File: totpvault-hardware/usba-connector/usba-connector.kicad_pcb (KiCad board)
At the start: 2 copper layers, 17.1 x 37.8 mm, 30 parts, among them J3 Conn_01x06_Socket, U1 ESP32-C3, U2 HT75xx-1-SOT89, U3 CH343P, U4 USBLC6-2SC6, Y1 Crystal_GND24

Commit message: Finalized PCB, added label and fixed solder mask
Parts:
- moved J3 1.10 mm to (99.0, 55.8)
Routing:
- net TXD_uC: track 23.8 -> 24.5 mm
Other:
- board text added: "PassVault v1.0"
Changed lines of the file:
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@@
 	(footprint "Connector_PinHeader_2.54mm:PinHeader_1x06_P2.54mm_Vertical"
 		(layer "F.Cu")
-		(at 98.975 56.85)
+		(at 99 55.75)
 		(descr "Through hole straight pin header, 1x06, 2.54mm pitch, single row")
 		(tags "Through hole pin header THT 1x06 2.54mm single row")
 		(property "Reference" "J3"
-			(at 0 -2.33 0)
+			(at -0.9 -2.25 0)
 			(layer "F.SilkS")
 			(effects
@@
 		(tags "SMD SMT crystal")
 		(property "Reference" "Y1"
-			(at 2.5 -2 0)
+			(at -0.2 2.15 0)
 			(layer "F.SilkS")
 			(effects
@@
 		(at 100.945 51.25 180)
 		(property "Reference" "U3"
-			(at 2.445 -0.25 270)
+			(at 2.445 0.05 90)
 			(layer "F.SilkS")
 			(effects
@@
 		(sheetname "/")
 		(sheetfile "usba-connector.kicad_sch")
+		(solder_mask_margin 0)
 		(attr smd)
 		(fp_line
@@
 			(pinfunction "VIO")
 			(pintype "power_in")
-			(solder_mask_margin 0.07)
+			(solder_mask_margin 0.01)
 			(clearance 0.07)
 		)
@@
 			(pinfunction "GND")
 			(pintype "power_in")
-			(solder_mask_margin 0.07)
+			(solder_mask_margin 0.01)
 			(clearance 0.07)
 		)
@@
 			(pinfunction "VDD5")
 			(pintype "power_in")
-			(solder_mask_margin 0.07)
+			(solder_mask_margin 0.01)
 			(clearance 0.07)
 		)
@@
 			(pinfunction "TXD")
 			(pintype "output")
-			(solder_mask_margin 0.07)
+			(solder_mask_margin 0.01)
 			(clearance 0.07)
 		)
@@
 			(pinfunction "RXD")
 			(pintype "input")
-			(solder_mask_margin 0.07)
+			(solder_mask_margin 0.01)
 			(clearance 0.07)
 		)
@@
 			(pinfunction "V3")
 			(pintype "power_in")
-			(solder_mask_margin 0.07)
+			(solder_mask_margin 0.01)
 			(clearance 0.07)
 		)
@@
 			(pinfunction "UD+")
 			(pintype "bidirectional")
-			(solder_mask_margin 0.07)
+			(solder_mask_margin 0.01)
 			(clearance 0.07)
 		)
@@
 			(pinfunction "UD-")
 			(pintype "bidirectional")
-			(solder_mask_margin 0.07)
+			(solder_mask_margin 0.01)
 			(clearance 0.07)
 		)
@@
 			(pinfunction "VBUS")
 			(pintype "input")
-			(solder_mask_margin 0.07)
+			(solder_mask_margin 0.01)
 			(clearance 0.07)
 		)
@@
 			(pinfunction "~{ACT}")
 			(pintype "output+no_connect")
-			(solder_mask_margin 0.07)
+			(solder_mask_margin 0.01)
 			(clearance 0.07)
 		)
@@
 			(pinfunction "DCD")
 			(pintype "input+no_connect")
-			(solder_mask_margin 0.07)
+			(solder_mask_margin 0.01)
 			(clearance 0.07)
 		)
@@
 			(pinfunction "DTR")
 			(pintype "output+no_connect")
-			(solder_mask_margin 0.07)
+			(solder_mask_margin 0.01)
 			(clearance 0.07)
 		)
@@
 			(pinfunction "RTS")
 			(pintype "output+no_connect")
-			(solder_mask_margin 0.07)
+			(solder_mask_margin 0.01)
 			(clearance 0.07)
 		)
@@
 			(pinfunction "DSR")
 			(pintype "input+no_connect")
-			(solder_mask_margin 0.07)
+			(solder_mask_margin 0.01)
 			(clearance 0.07)
 		)
@@
 			(pinfunction "CTS")
 			(pintype "input+no_connect")
-			(solder_mask_margin 0.07)
+			(solder_mask_margin 0.01)
 			(clearance 0.07)
 		)
@@
 			(pinfunction "RI")
 			(pintype "input+no_connect")
-			(solder_mask_margin 0.07)
+			(solder_mask_margin 0.01)
 			(clearance 0.07)
 		)
@@
 			(pinfunction "GND__1")
 			(pintype "power_in")
-			(solder_mask_margin 0.07)
+			(solder_mask_margin 0)
 			(clearance 0.07)
 		)
@@
 		(tags "LED")
 		(property "Reference" "D1"
-			(at 1.975 0 90)
+			(at -0.3 1.275 90)
 			(layer "F.SilkS")
 			(effects
@@
 		(layer "Edge.Cuts")
 	)
+	(gr_text "PassVault v1.0"
+		(at 101.3 71 0)
+		(layer "F.SilkS")
+		(effects
+			(font
+				(size 0.8 0.8)
+				(thickness 0.16)
+				(bold yes)
+			)
+			(justify left bottom)
+		)
+	)
 	(segment
 		(start 103.205 48.125)
@@
 	)
 	(segment
+		(start 104.758944 54.65)
+		(end 105.616972 53.791972)
+		(width 0.5)
+		(layer "F.Cu")
+		(net 6)
+	)
+	(segment
 		(start 107.545 55.875)
 		(end 107.545 53.685)
@@
 	)
 	(segment
-		(start 108.25 51.375)
-		(end 109.575 52.7)
+		(start 102.375 54.65)
+		(end 104.758944 54.65)
 		(width 0.5)
 		(layer "F.Cu")
@@
 	)
 	(segment
-		(start 98.975 59.39)
-		(end 101.1 57.265)
+		(start 108.25 51.375)
+		(end 109.575 52.7)
 		(width 0.5)
 		(layer "F.Cu")
@@
 	)
 	(segment
-		(start 101.1 57.265)
-		(end 101.1 55.925)
-		(width 0.5)
+		(start 104.345 52.52)
+		(end 105.616972 53.791972)
+		(width 0.2)
 		(layer "F.Cu")
 		(net 6)
 	)
 	(segment
-		(start 104.345 52.52)
-		(end 105.616972 53.791972)
-		(width 0.2)
+		(start 101.1 57.265)
+		(end 100.025 57.265)
+		(width 0.5)
 		(layer "F.Cu")
 		(net 6)
@@
 	)
 	(segment
-		(start 104.758944 54.65)
-		(end 105.616972 53.791972)
+		(start 100.025 57.265)
+		(end 99 58.29)
 		(width 0.5)
 		(layer "F.Cu")
@@
 	)
 	(segment
+		(start 101.1 57.265)
+		(end 101.1 55.925)
+		(width 0.5)
+		(layer "F.Cu")
+		(net 6)
+	)
+	(segment
 		(start 112.525 68.8375)
 		(end 111.1625 68.8375)
@@
 	)
 	(segment
-		(start 102.375 54.65)
-		(end 104.758944 54.65)
+		(start 101.535 57.7)
+		(end 101.1 57.265)
+		(width 0.2)
+		(layer "F.Cu")
+		(net 6)
+	)
+	(segment
+		(start 101.1 55.925)
+		(end 102.375 54.65)
 		(width 0.5)
 		(layer "F.Cu")
@@
 	)
 	(segment
-		(start 101.535 57.7)
-		(end 101.1 57.265)
-		(width 0.2)
-		(layer "F.Cu")
-		(net 6)
-	)
-	(segment
 		(start 108.5 61)
 		(end 110.67 61)
@@
 	)
 	(segment
-		(start 101.1 55.925)
-		(end 102.375 54.65)
-		(width 0.5)
-		(layer "F.Cu")
-		(net 6)
-	)
-	(segment
 		(start 108.25 45.525)
 		(end 108.25 51.375)
@@
 	)
 	(segment
-		(start 99.225 69.8)
-		(end 98.975 69.55)
+		(start 100.35 69.8)
+		(end 99 68.45)
 		(width 0.2)
 		(layer "B.Cu")
@@
 	(segment
 		(start 111.15 69.8)
-		(end 99.225 69.8)
+		(end 100.35 69.8)
 		(width 0.2)
 		(layer "B.Cu")
@@
 	)
 	(segment
+		(start 99.827179 64.197179)
+		(end 99 63.37)
+		(width 0.2)
+		(layer "F.Cu")
+		(net 10)
+	)
+	(segment
 		(start 103.6 49.125)
 		(end 102.375 49.125)
@@
 	)
 	(segment
-		(start 102.659764 64.25)
-		(end 99.195 64.25)
+		(start 102.712585 64.197179)
+		(end 99.827179 64.197179)
 		(width 0.2)
 		(layer "F.Cu")
@@
 	)
 	(segment
-		(start 99.195 64.25)
-		(end 98.975 64.47)
-		(width 0.2)
-		(layer "F.Cu")
-		(net 10)
-	)
-	(segment
 		(start 105.7135 62.8786)
 		(end 105.7135 62.874)
@@
 	)
 	(segment
-		(start 101.75 56.65)
-		(end 101.75 64.235)
+		(start 101.75 64.25)
+		(end 101.75 56.65)
 		(width 0.2)
 		(layer "B.Cu")
@@
 	)
 	(segment
-		(start 102.4 56)
-		(end 101.75 56.65)
+		(start 99 65.91)
+		(end 100.09 65.91)
 		(width 0.2)
 		(layer "B.Cu")
@@
 	(segment
 		(start 103.275 56)
-		(end 102.4 56)
+		(end 103.55 55.725)
+		(width 0.2)
+		(layer "B.Cu")
+		(net 11)
+	)
+	(segment
+		(start 100.09 65.91)
+		(end 101.75 64.25)
 		(width 0.2)
 		(layer "B.Cu")
@@
 	)
 	(segment
-		(start 101.75 64.235)
-		(end 98.975 67.01)
+		(start 101.75 56.65)
+		(end 102.4 56)
 		(width 0.2)
 		(layer "B.Cu")
@@
 	)
 	(segment
-		(start 103.55 55.725)
+		(start 102.4 56)
 		(end 103.275 56)
 		(width 0.2)
@@
 	)
 	(segment
-		(start 105.3125 62.7125)
-		(end 105.3125 62.1875)
+		(start 103.5 63.45)
+		(end 101.05 63.45)
 		(width 0.2)
 		(layer "F.Cu")
@@
 	)
 	(segment
-		(start 100.495 63.45)
-		(end 98.975 61.93)
+		(start 105.3125 62.7125)
+		(end 105.3125 62.1875)
 		(width 0.2)
 		(layer "F.Cu")
@@
 	)
 	(segment
+		(start 99 61.4)
+		(end 99 60.83)
+		(width 0.2)
+		(layer "F.Cu")
+		(net 43)
+	)
+	(segment
 		(start 103.5 63.45)
 		(end 104.575 63.45)
@@
 	)
 	(segment
-		(start 103.5 63.45)
-		(end 100.495 63.45)
+		(start 101.05 63.45)
+		(end 99 61.4)
 		(width 0.2)
 		(layer "F.Cu")

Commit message: PCB Order
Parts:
- removed R2: 499, Resistor_SMD:R_0402_1005Metric
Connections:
- J3 pad 3: TXD_uC -> TXD
- U1 pad 27: TXD_uC -> TXD
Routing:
- net TXD: track 1.59 -> 26.2 mm, vias 0 -> 2
- net TXD_uC: track 24.5 -> 0.00 mm, vias 2 -> 0
- net VBUS: track 55.1 -> 56.0 mm

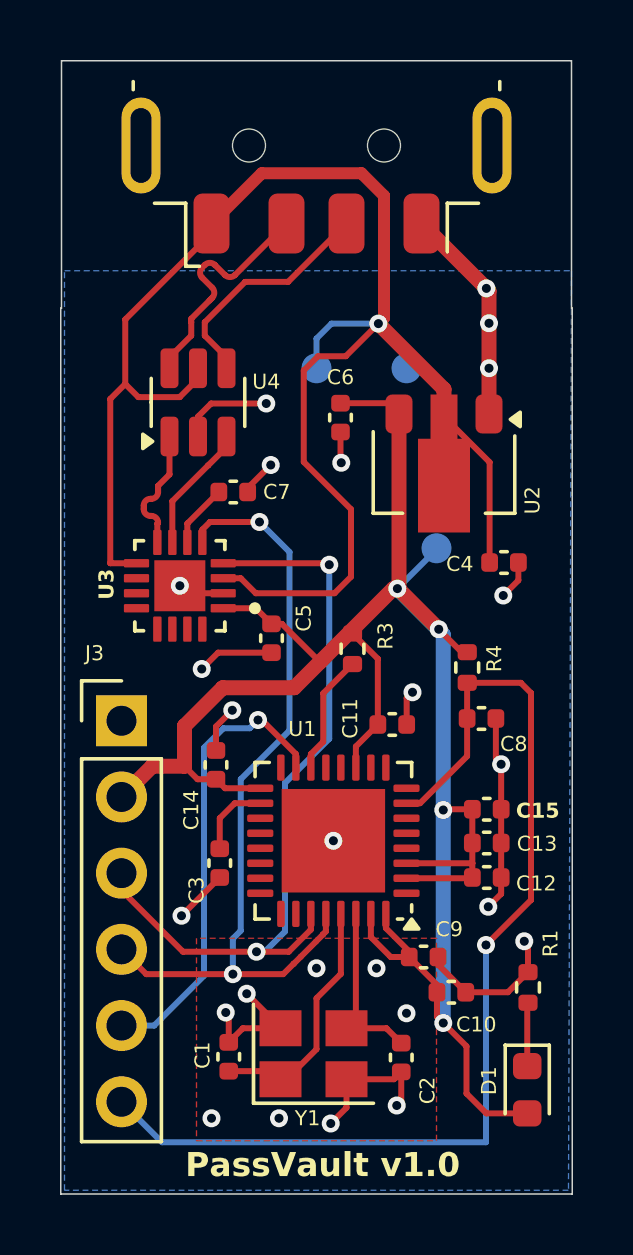
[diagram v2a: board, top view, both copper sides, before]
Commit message: Finalized new board design with JLCPCB basic parts, code cleanup
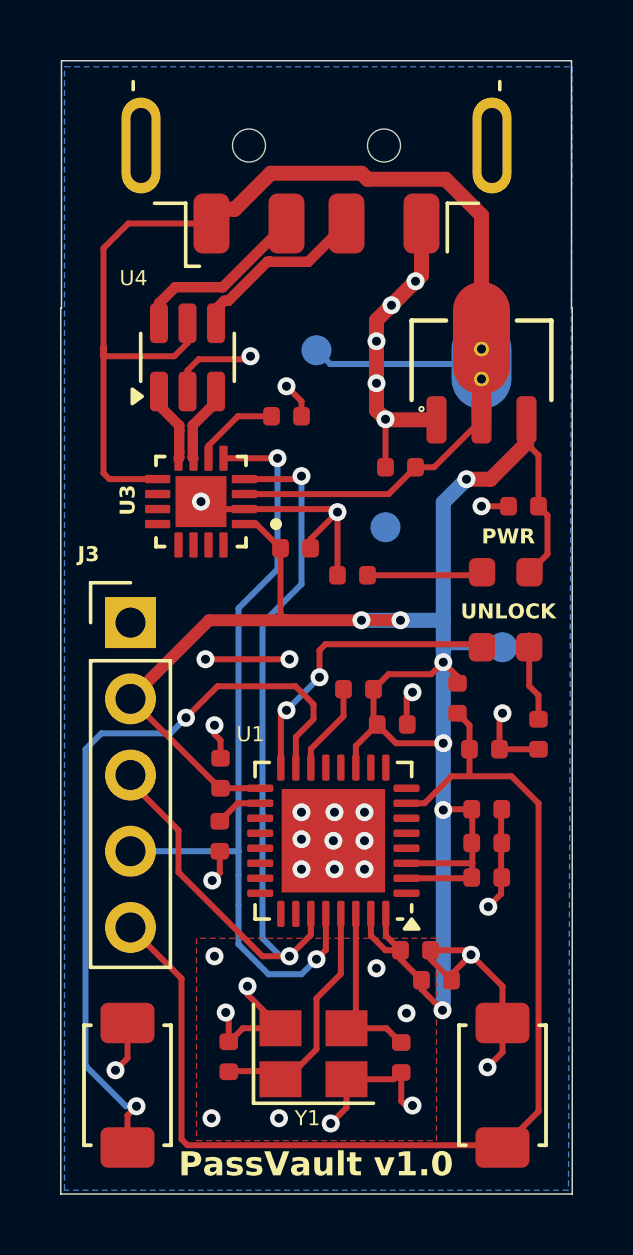
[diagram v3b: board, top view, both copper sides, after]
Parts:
- added D2: KT-0603R, PCM_JLCPCB:D_0603, F.Cu at (111.8, 53.3)
- added R2: 120, PCM_JLCPCB:R_0402, F.Cu at (112.9, 56.2)
- added S1: DFU Tactile Button, 160gf, PCM_JLCPCB:SW_TS-1088-AR02016, F.Cu at (99.2, 67.9)
- added S2: Reset Tactile Button, 160gf, PCM_JLCPCB:SW_TS-1088-AR02016, F.Cu at (111.7, 67.9)
- C1, C10, C11, C12, C13, C14, C15, C2, C3, C4, C5, C6, C7, C8, C9: footprint Capacitor_SMD:C_0402_1005Metric -> PCM_JLCPCB:C_0402
- D1: footprint LED_SMD:LED_0603_1608Metric -> PCM_JLCPCB:D_0603
- J3: value Conn_01x06_Socket -> Conn_01x05_Socket; footprint Connector_PinHeader_2.54mm:PinHeader_1x06_P2.54mm_Vertical -> Connector_PinHeader_2.54mm:PinHeader_1x05_P2.54mm_Vertical
- R1: value 100 -> 120; footprint Resistor_SMD:R_0402_1005Metric -> PCM_JLCPCB:R_0402
- R3, R4: footprint Resistor_SMD:R_0402_1005Metric -> PCM_JLCPCB:R_0402
- U2: footprint Package_TO_SOT_SMD:SOT-89-3 -> PCM_JLCPCB:SOT-89-3_L4.5-W2.5-P1.50-LS4.2-BR
- moved D1 17.3 mm to (111.8, 50.8), turned to 0 degrees
- moved R1 14.9 mm to (106.7, 50.9), turned to 0 degrees
- moved C6 6.78 mm to (112.4, 48.6), turned to 180 degrees
- moved TP2 5.35 mm to (107.8, 49.3)
- moved C4 4.69 mm to (108.3, 47.3), turned to 180 degrees
- moved TP3 3.97 mm to (111.7, 53.3)
- moved U2 3.36 mm to (111.0, 44.4)
- moved J3 3.28 mm to (99.3, 52.5)
- moved C5 3.10 mm to (104.8, 50.0), turned to 0 degrees
- moved C7 3.09 mm to (104.5, 45.6)
- moved U3 2.89 mm to (101.7, 48.4)
- moved U4 1.54 mm to (101.2, 43.6)
- moved R3 1.36 mm to (106.9, 54.7), turned to 180 degrees
- moved R4 1.08 mm to (110.2, 55.0)
- moved C8 1.03 mm to (111.1, 56.7)
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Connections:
- J3 pad 5: BOOT -> RESET
- U1 pad 16: unconnected-(U1-GPIO10-Pad16) -> Net-(U1-GPIO10)
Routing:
- net GND: track 43.5 -> 56.0 mm, vias 25 -> 38
- net Net-(U1-GPIO10): track 0.00 -> 9.98 mm, vias 0 -> 2
- net BOOT: track 15.4 -> 25.4 mm, vias 1 -> 2
- net VBUS: track 56.0 -> 46.6 mm, vias 1 -> 0
- net TXD: track 26.2 -> 29.5 mm
- net Net-(D2-Pad1): track 0.00 -> 2.97 mm
- net RESET: track 35.7 -> 38.0 mm, vias 1 -> 0
- net Net-(D1-Pad1): track 2.12 -> 4.14 mm
- net /D+: track 7.92 -> 6.01 mm
- net /D-: track 7.89 -> 6.02 mm
- net /EMI_D+: track 4.28 -> 2.56 mm
- net /EMI_D-: track 4.23 -> 2.51 mm
- net Net-(U1-VDD_SPI/GPIO11): track 2.57 -> 1.60 mm
- net Net-(U1-GPIO8): track 4.03 -> 3.06 mm
- net VDD3P3: track 72.3 -> 73.1 mm, vias 4 -> 7
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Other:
- board text added: "3v3"
- board text added: "GND"
- board text added: "PWR"
- board text added: "RST"
- board text added: "RX"
- board text added: "TX"
- board text added: "UNLOCK"

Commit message: Updated documentation with schematics and images, delete GUI project, PCB 3D design cleanup
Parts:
- R1, R2: value 120 -> 400
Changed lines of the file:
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@@
 			(layer "F.Mask"
 				(type "Top Solder Mask")
+				(color "Black")
 				(thickness 0.01)
 			)
@@
 			(layer "B.Mask"
 				(type "Bottom Solder Mask")
+				(color "Black")
 				(thickness 0.01)
 			)
@@
 		(embedded_fonts no)
 		(model "${KICAD9_3DMODEL_DIR}/Connector_PinHeader_2.54mm.3dshapes/PinHeader_1x05_P2.54mm_Vertical.wrl"
+			(hide yes)
 			(offset
 				(xyz 0 0 0)
@@
 			)
 		)
-		(property "Value" "120"
+		(property "Value" "400"
 			(at 0 0.2 90)
 			(layer "F.Fab")
@@
 			)
 		)
-		(property "Value" "120"
+		(property "Value" "400"
 			(at 0 0.2 0)
 			(layer "F.Fab")

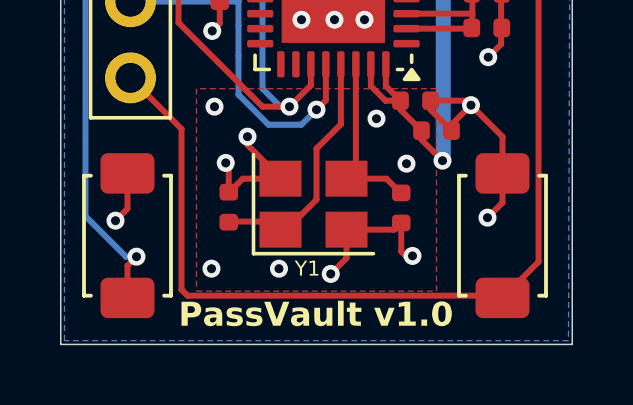
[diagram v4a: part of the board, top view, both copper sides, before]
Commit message: Migrated to Argon2id for KDF, fixed potential panics, added additional zeroize of regions, code formatting cleanup
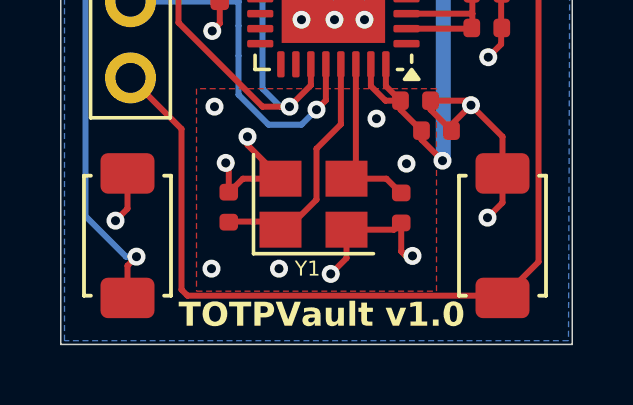
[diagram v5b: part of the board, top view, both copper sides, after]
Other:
- board text added: "TOTPVault v1.0"
- board text removed: "PassVault v1.0"
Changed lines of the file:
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@@
 			(psa4output no)
 			(plot_black_and_white yes)
-			(plotinvisibletext no)
 			(sketchpadsonfab no)
 			(plotpadnumbers no)
@@
 			(layer "F.Fab")
 		)
-		(fp_text user "${REFERENCE}"
-			(at 0 -0.25 270)
-			(layer "F.Fab")
-			(hide yes)
-			(effects
-				(font
-					(size 0.25 0.25)
-					(thickness 0.04)
-				)
-			)
-		)
 		(pad "1" smd roundrect
 			(at -0.5 0 270)
@@
 			(layer "F.Fab")
 		)
-		(fp_text user "${REFERENCE}"
-			(at 0 -0.25 90)
-			(layer "F.Fab")
-			(hide yes)
-			(effects
-				(font
-					(size 0.25 0.25)
-					(thickness 0.04)
-				)
-			)
-		)
 		(pad "1" smd roundrect
 			(at -0.5 0 90)
@@
 			(layer "F.Fab")
 		)
-		(fp_text user "${REFERENCE}"
-			(at 0 -0.25 0)
-			(layer "F.Fab")
-			(hide yes)
-			(effects
-				(font
-					(size 0.25 0.25)
-					(thickness 0.04)
-				)
-			)
-		)
 		(pad "1" smd roundrect
 			(at -0.5 0)
@@
 			(layer "F.Fab")
 		)
-		(fp_text user "${REFERENCE}"
-			(at 0 -0.25 0)
-			(layer "F.Fab")
-			(hide yes)
-			(effects
-				(font
-					(size 0.25 0.25)
-					(thickness 0.04)
-				)
-			)
-		)
 		(pad "1" smd roundrect
 			(at -0.5 0 180)
@@
 		)
 	)
-	(gr_text "PassVault v1.0"
+	(gr_text "TOTPVault v1.0"
 		(at 100.9 71 0)
 		(layer "F.SilkS")
